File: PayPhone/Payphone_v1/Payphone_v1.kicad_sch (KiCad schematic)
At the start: 86 parts, among them J1 JST_05, J2 Molex_26-60-4030, J3 Molex_26-60-4040, J6 PINHD_1x5_Male, J7 PINHD_1x2_Male, J8 PINHD_1x2_Male, J9 PINHD_1x2_Male, K1 G6S-2, Q2 2N7000, Q3 IRF630, Q4 2N7000, Q5 2N7000, Q6 2N3906, U1 MCP23008-xP, U2 MC34063AP, U3 UC3843AN, U4 ADS1115IDGS

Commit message: Payphone_v1: U3 = UC3843BNG (onsemi UC3843AN obsolete); U4 ADS1115 fixed (VDD to 3.3 V, ADDR to GND, AIN1 divider 56k/10k, C17), ISENSE on AIN2; docs: THT vs SMT price comparison with Extended-fee recommendation, wiring guide matches R20-R26
Co-Authored-By: Claude Opus 5.5 <noreply@anthropic.com>
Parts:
- added C17: 0.1uF, Capacitor_THT:C_Disc_D5.0mm_W2.5mm_P5.00mm, symbol Device:C_Small
- R17: value 33k -> 56k
- R19: value 33k -> 10k
- U3: value UC3843AN -> UC3843BNG
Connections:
- net +3V3: now also U4.8 (VDD), C17.1
- net +5V: no longer U4.8 (VDD)
- net GND: now also U4.1 (ADDR), C17.2

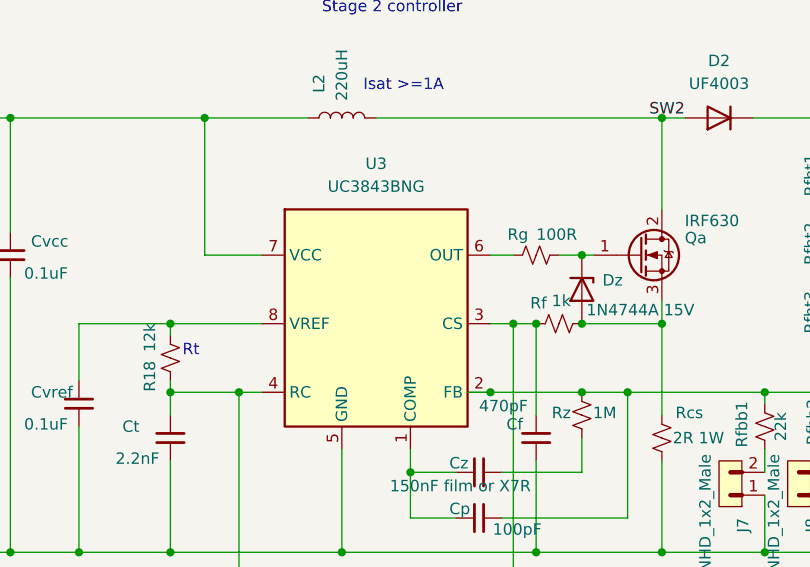
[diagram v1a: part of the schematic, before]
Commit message: Payphone_v1: remove stray wire stub near U3; U3 back to UC3843AN (TI); SMT doc: UC3843 surface-mount options (UC3843BD1R2G, UCC38C43DR, UCC28C43)
Co-Authored-By: Claude Opus 5.5 <noreply@anthropic.com>
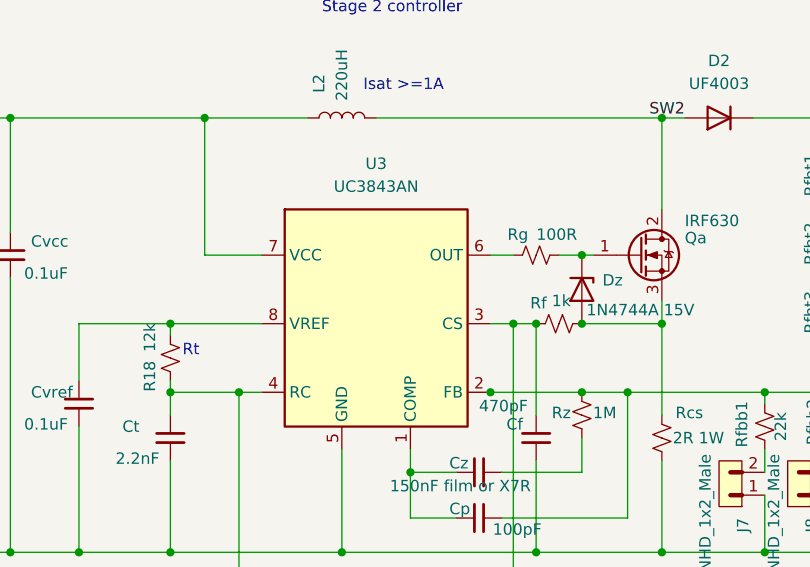
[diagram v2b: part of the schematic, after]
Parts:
- U3: value UC3843BNG -> UC3843AN
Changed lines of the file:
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@@
-	(wire
-		(pts
-			(xy 95.25 128.27) (xy 97.79 128.27)
-		)
-		(stroke
-			(width 0)
-			(type default)
-		)
-	)
 	(wire
 		(pts
@@
 			)
 		)
-		(property "Value" "UC3843BNG"
+		(property "Value" "UC3843AN"
 			(at 85.09 105.41 0)
 			(show_name no)
